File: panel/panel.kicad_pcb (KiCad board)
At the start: 4 copper layers, 36 x 36 mm, 289 parts, among them J1 IN, J2 OUT, Q1 Q_PMOS_GSD, Q10 Q_PMOS_GSD, Q11 Q_PMOS_GSD, Q12 Q_PMOS_GSD, Q13 Q_PMOS_GSD, Q14 Q_PMOS_GSD, Q15 Q_PMOS_GSD, Q16 Q_PMOS_GSD, Q2 Q_PMOS_GSD, Q3 Q_PMOS_GSD, Q4 Q_PMOS_GSD, Q5 Q_PMOS_GSD, Q6 Q_PMOS_GSD, Q7 Q_PMOS_GSD, Q8 Q_PMOS_GSD, Q9 Q_PMOS_GSD, U1 TLC59025, U2 TLC59025, U3 TLC59025, U4 SN74HC595, U5 SN74HC595, U6 NC7WZ17, U7 NC7WZ17

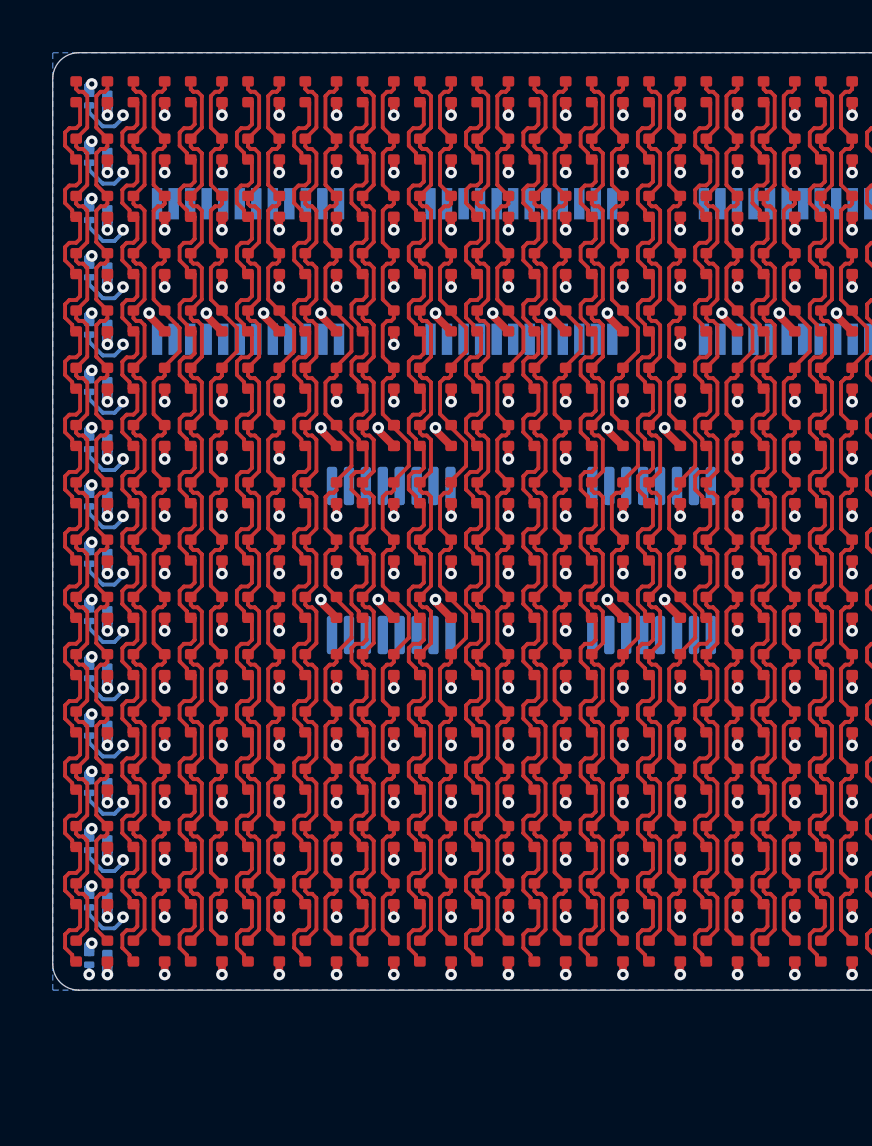
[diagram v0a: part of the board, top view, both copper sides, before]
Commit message: First option for row MOSFET layout
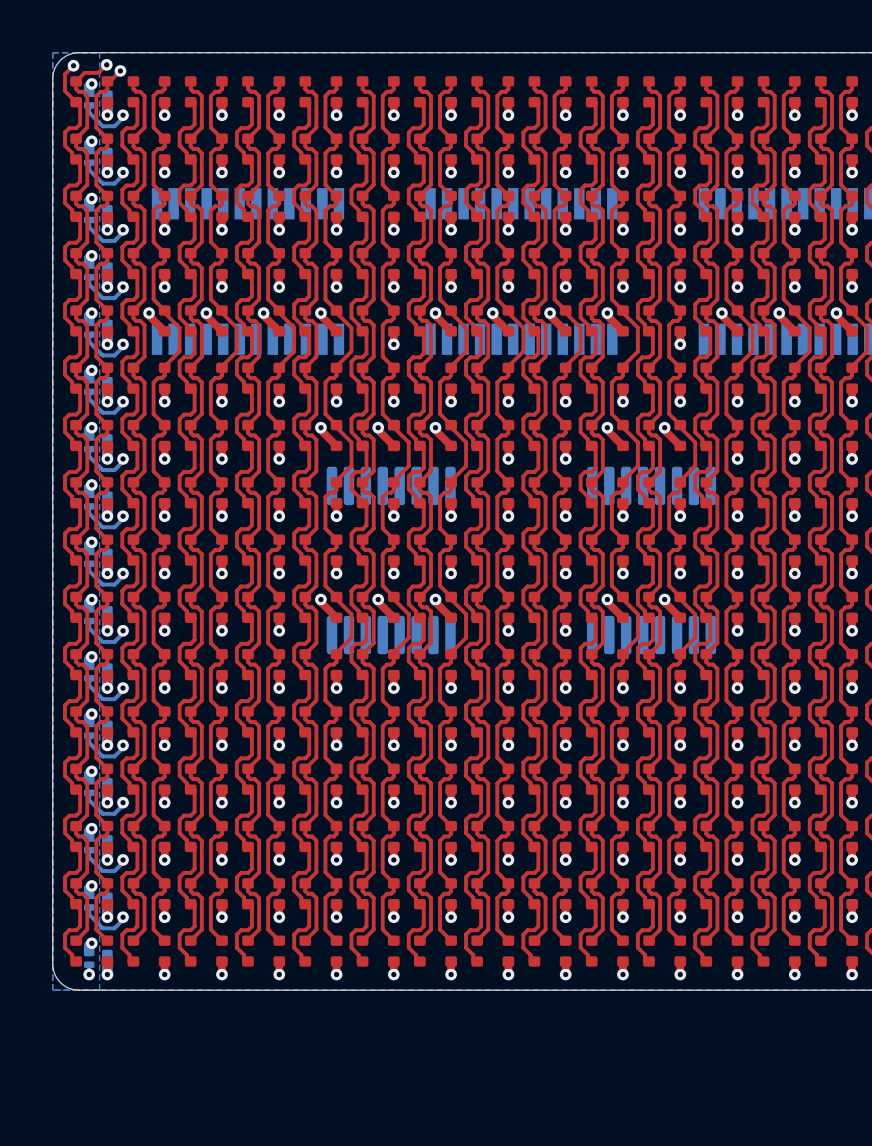
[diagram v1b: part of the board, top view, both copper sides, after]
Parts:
- turned U5 to 90 degrees
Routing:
- net COL_0B: track 45.1 -> 46.8 mm, vias 0 -> 1
- net COL_0G: track 39.7 -> 41.2 mm, vias 0 -> 1
- net COL_0R: track 39.7 -> 40.4 mm, vias 0 -> 1
- added copper zone on B.Cu, net VCC
- removed copper zone on In2.Cu, net VCC

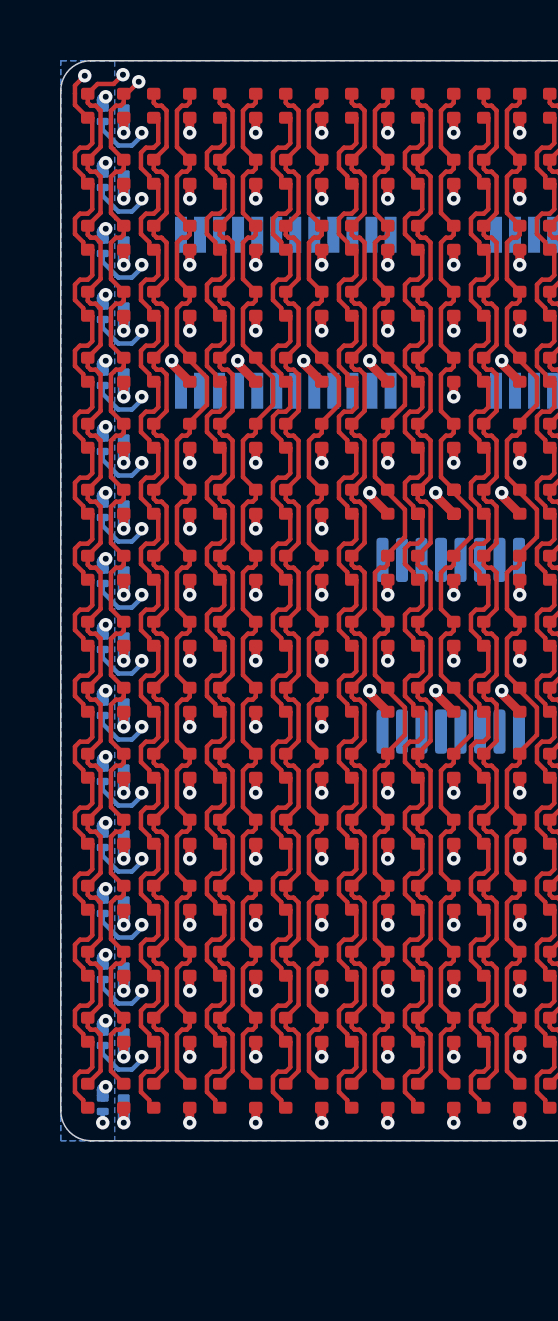
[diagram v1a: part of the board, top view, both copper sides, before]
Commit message: New strategy for powering rows
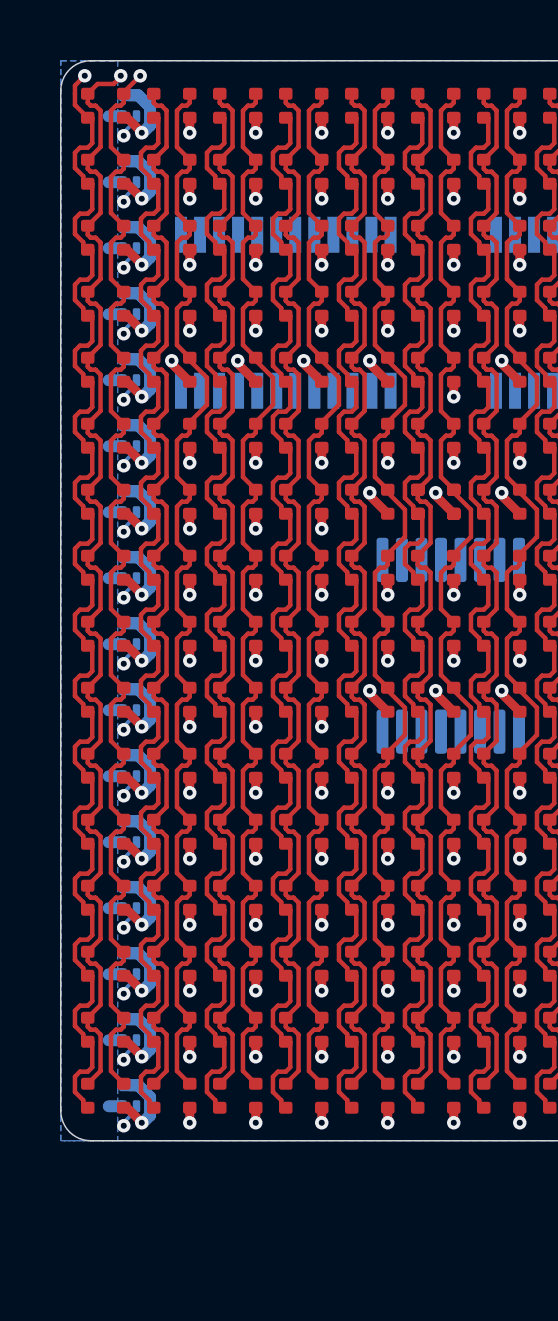
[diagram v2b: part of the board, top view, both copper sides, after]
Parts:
- moved Q14 0.63 mm to (62.3, 90.1), turned to 90 degrees
- moved Q4 0.63 mm to (62.3, 68.1), turned to 90 degrees
- moved Q9 0.63 mm to (62.3, 79.1), turned to 90 degrees
- moved Q1 0.63 mm to (62.3, 61.5), turned to 90 degrees
- moved Q10 0.63 mm to (62.3, 81.3), turned to 90 degrees
- moved Q11 0.63 mm to (62.3, 83.5), turned to 90 degrees
- moved Q12 0.63 mm to (62.3, 85.7), turned to 90 degrees
- moved Q13 0.63 mm to (62.3, 87.9), turned to 90 degrees
- moved Q15 0.63 mm to (62.3, 92.3), turned to 90 degrees
- moved Q16 0.63 mm to (62.3, 94.5), turned to 90 degrees
- moved Q2 0.63 mm to (62.3, 63.7), turned to 90 degrees
- moved Q3 0.63 mm to (62.3, 65.9), turned to 90 degrees
- moved Q5 0.63 mm to (62.3, 70.3), turned to 90 degrees
- moved Q6 0.63 mm to (62.3, 72.5), turned to 90 degrees
- moved Q7 0.63 mm to (62.3, 74.7), turned to 90 degrees
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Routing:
- net /ROW_8: track 2.03 -> 0.83 mm
- net /ROW_3: track 2.03 -> 0.83 mm
- net /ROW_13: track 2.03 -> 0.83 mm
- net /ROW_0: track 2.03 -> 0.83 mm
- net /ROW_7: track 2.03 -> 0.83 mm
- net /ROW_6: track 2.03 -> 0.83 mm
- net /ROW_2: track 2.03 -> 0.83 mm
- net /ROW_12: track 2.03 -> 0.83 mm
- net /ROW_11: track 2.03 -> 0.83 mm
- net /ROW_1: track 2.03 -> 0.83 mm
- net /ROW_9: track 2.03 -> 0.83 mm
- net /ROW_4: track 2.03 -> 0.83 mm
- net /ROW_14: track 2.03 -> 0.83 mm
- net /ROW_5: track 2.03 -> 0.83 mm
- net /ROW_10: track 2.03 -> 0.83 mm
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
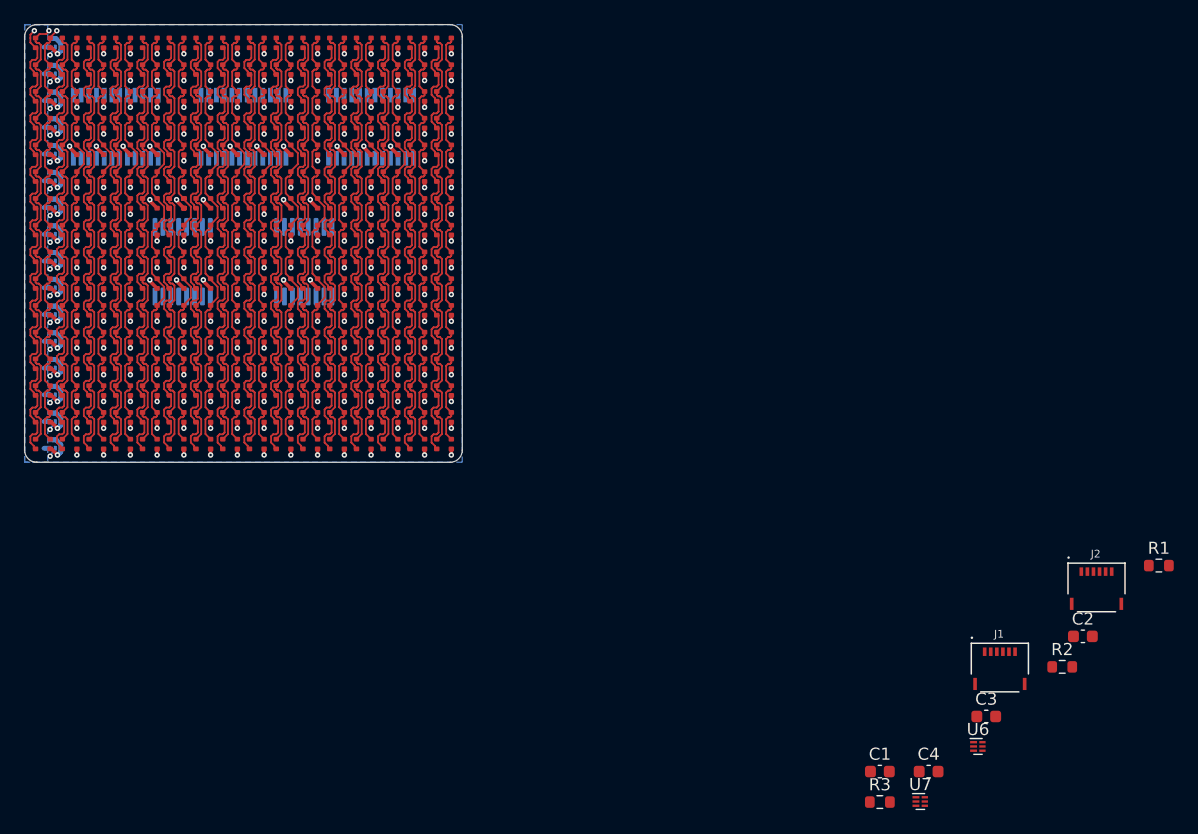
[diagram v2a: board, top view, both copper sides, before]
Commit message: Row gates 0-7 routed
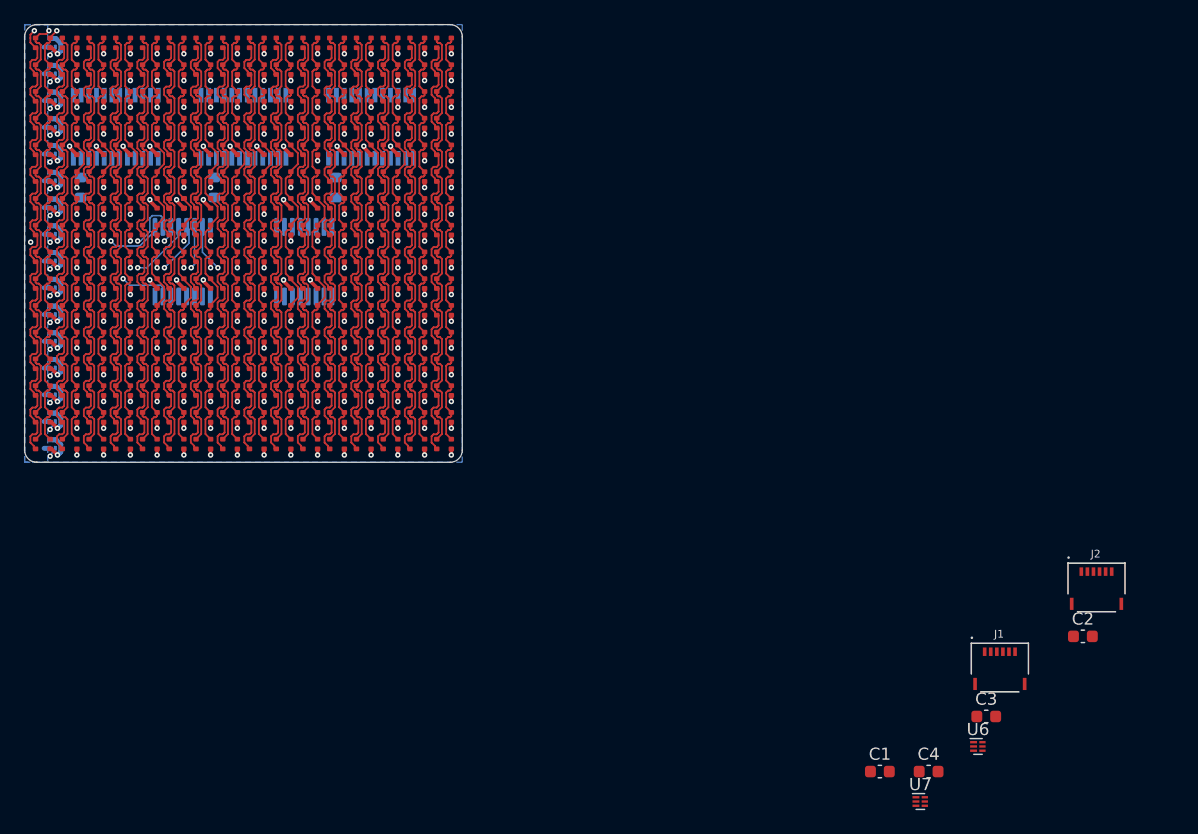
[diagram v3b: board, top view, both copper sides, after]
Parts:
- R1, R2, R3: moved to B.Cu
- moved R3 82.9 mm to (64.6, 73.4), turned to -90 degrees
- moved R2 80.1 mm to (75.6, 73.4), turned to -90 degrees
- moved R1 74.5 mm to (85.6, 73.4), turned to -90 degrees
- turned U4 to -90 degrees
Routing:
- net /ROW_0: track 0.83 -> 30.8 mm, vias 1 -> 3
- net /ROW_1: track 0.83 -> 23.9 mm, vias 1 -> 2
- net /ROW_2: track 0.83 -> 23.2 mm, vias 1 -> 2
- net /ROW_4: track 0.83 -> 22.2 mm, vias 1 -> 2
- net /ROW_5: track 0.83 -> 20.9 mm, vias 1 -> 2
- net /ROW_3: track 0.83 -> 19.8 mm, vias 1 -> 2
- net /ROW_6: track 0.83 -> 19.7 mm, vias 1 -> 2
- net /ROW_7: track 0.83 -> 19.5 mm, vias 1 -> 2

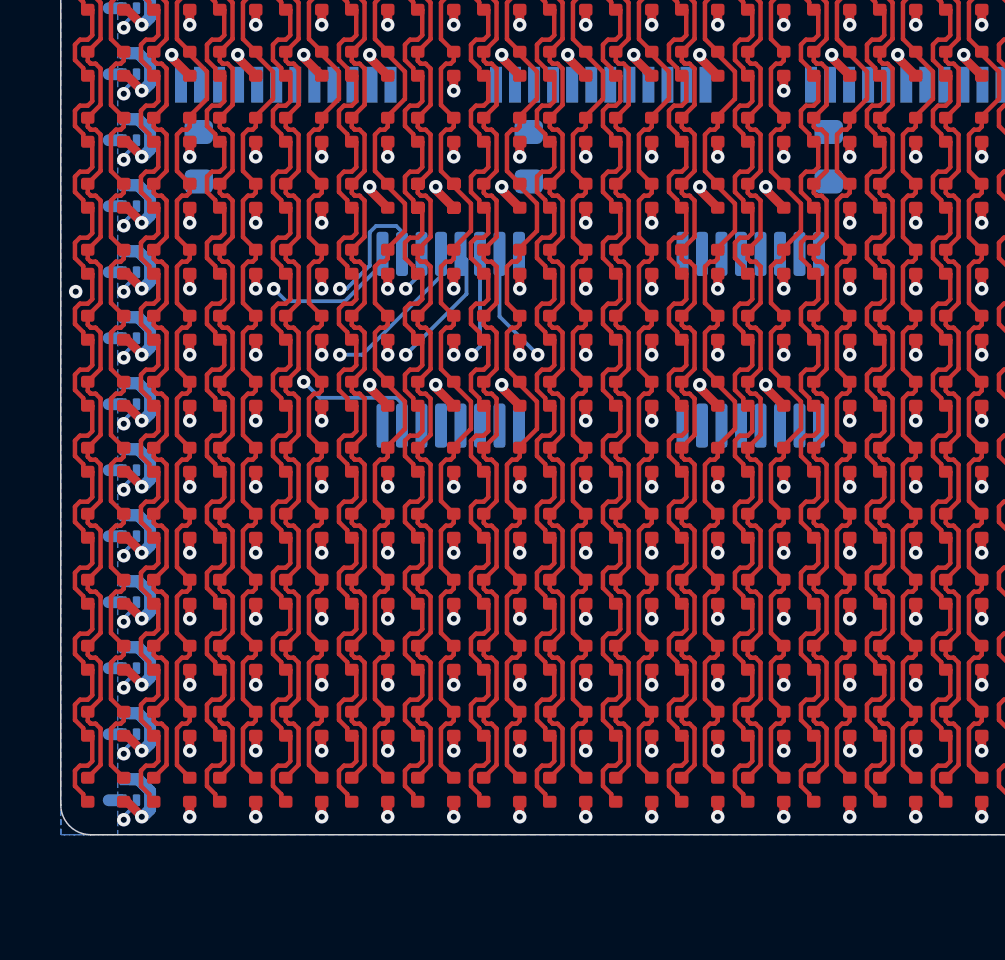
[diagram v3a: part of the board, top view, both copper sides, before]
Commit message: Rerouted first half of row drivers
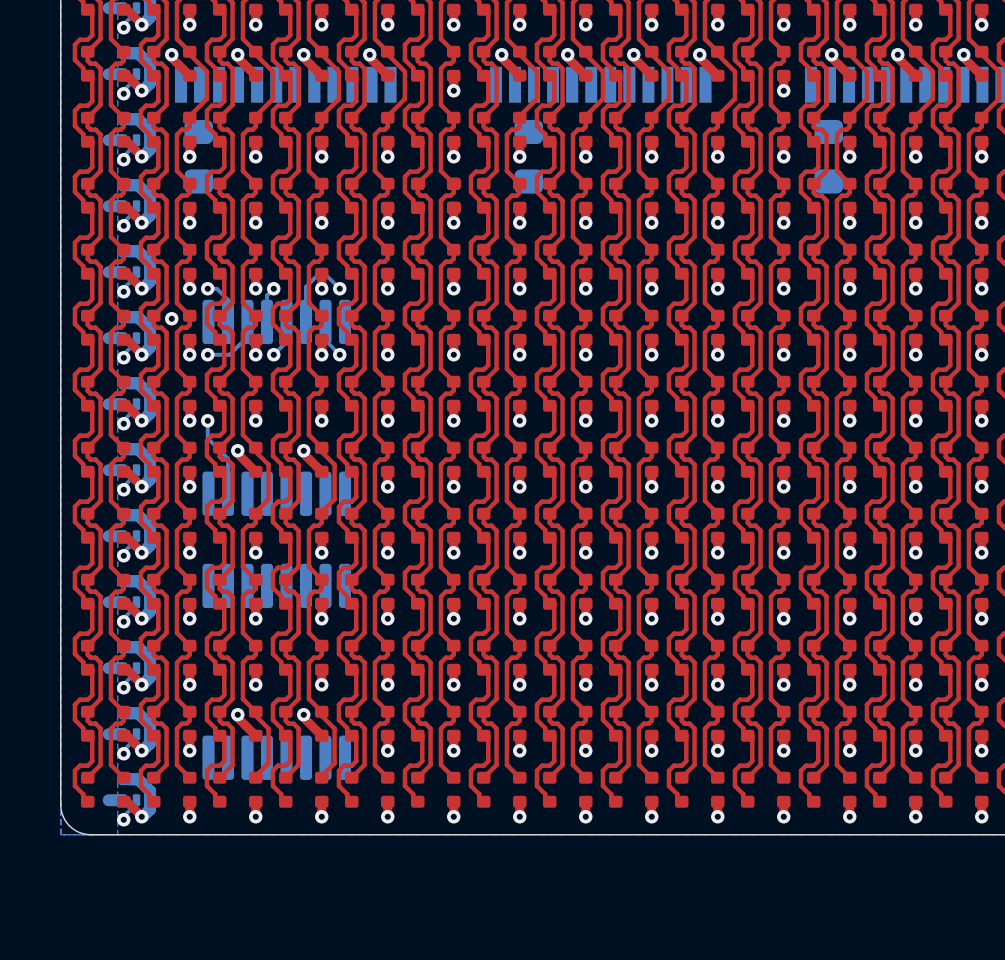
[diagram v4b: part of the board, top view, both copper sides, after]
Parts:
- moved U5 19.3 mm to (67.2, 90.6), turned to -90 degrees
- moved U4 6.23 mm to (67.2, 81.8)
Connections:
- U4 pad 10: VCC -> /ROW_9/COMMON
- U4 pad 11: /CLK -> /ROW_9/COMMON
- U4 pad 14: /DAT -> /ROW_9/COMMON
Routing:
- net /ROW_4: track 22.2 -> 13.1 mm
- net /ROW_6: track 19.7 -> 11.7 mm
- net /ROW_5: track 20.9 -> 13.1 mm
- net /ROW_7: track 19.5 -> 12.0 mm
- net /ROW_2: track 23.2 -> 16.0 mm
- net /ROW_1: track 23.9 -> 17.1 mm
- net /ROW_0: track 30.8 -> 25.6 mm, vias 3 -> 2
- net /ROW_3: track 19.8 -> 16.5 mm

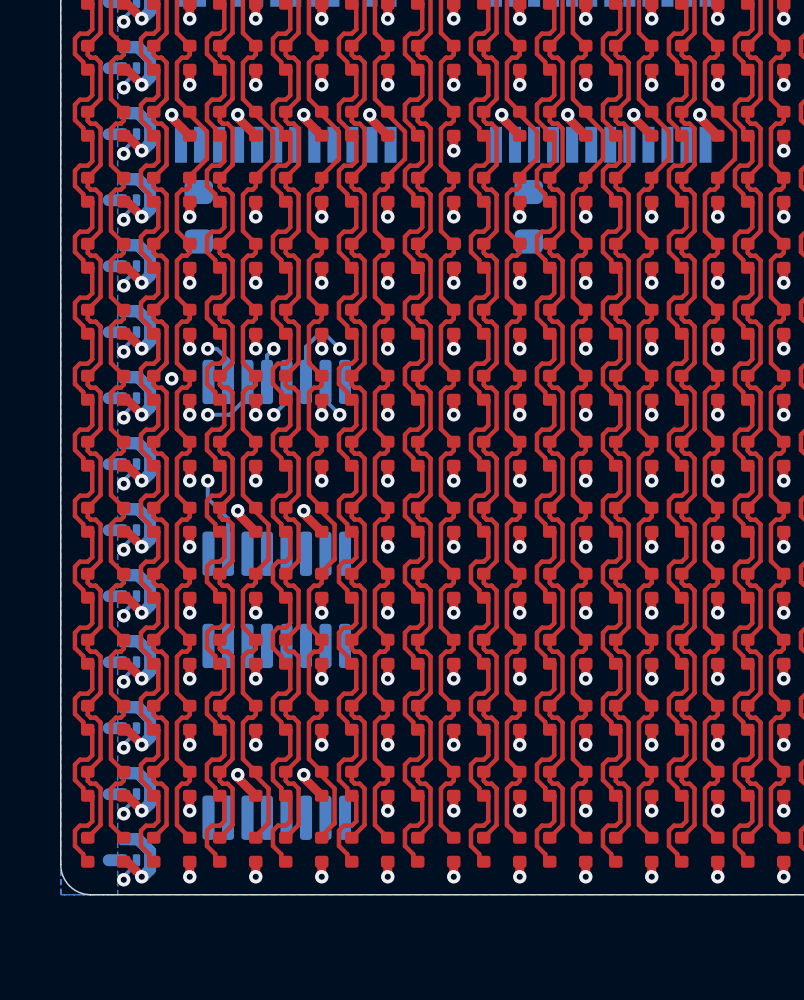
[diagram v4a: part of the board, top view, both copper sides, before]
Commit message: Routed second half of row drivers
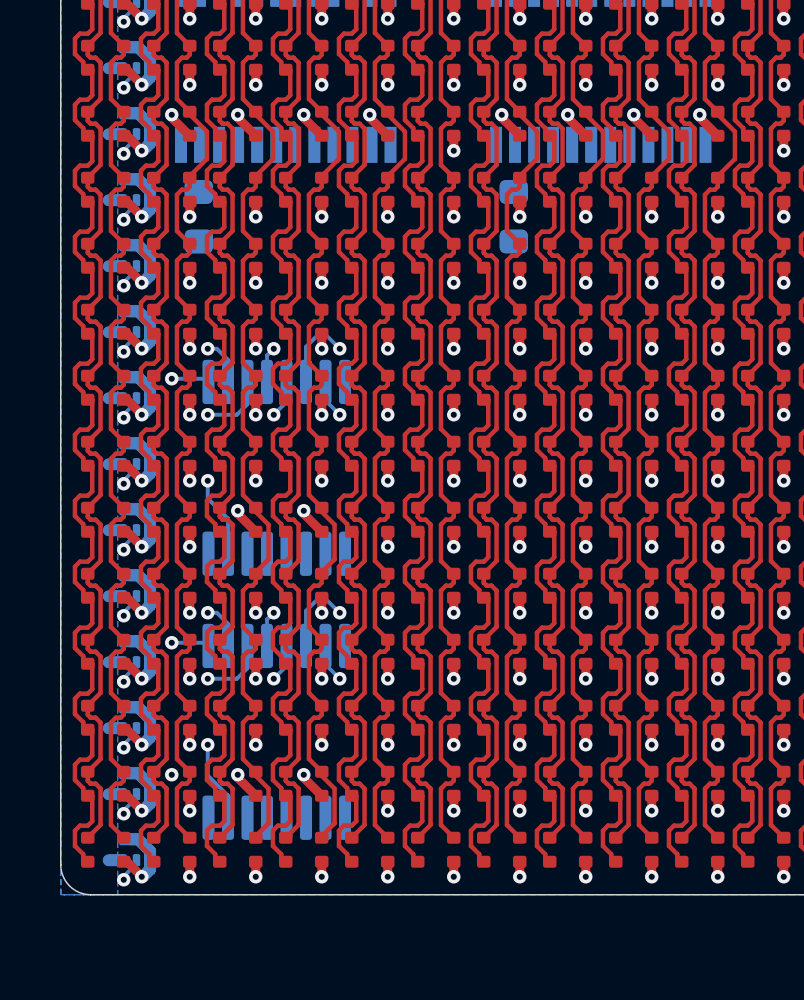
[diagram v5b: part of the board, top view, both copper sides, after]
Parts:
- removed the D102 at (72.5, 74.7)
- moved R2 0.50 mm to (75.1, 73.4)
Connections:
- U4 pad 10: /ROW_9/COMMON -> VCC
- U4 pad 11: /ROW_9/COMMON -> /CLK
- U4 pad 14: /ROW_9/COMMON -> /DAT
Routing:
- net /ROW_8: track 0.83 -> 24.8 mm, vias 1 -> 2
- net /ROW_15: track 0.83 -> 17.6 mm, vias 1 -> 2
- net /ROW_14: track 0.83 -> 14.1 mm, vias 1 -> 3
- net /ROW_13: track 0.83 -> 10.4 mm, vias 1 -> 2
- net /ROW_9: track 0.83 -> 9.16 mm, vias 1 -> 2
- net /ROW_12: track 0.83 -> 8.58 mm, vias 1 -> 2
- net /ROW_10: track 0.83 -> 6.90 mm, vias 1 -> 2
- net /ROW_11: track 0.83 -> 6.71 mm, vias 1 -> 2
- net /ROW_7: track 12.0 -> 10.2 mm
- net /ROW_1: track 17.1 -> 18.4 mm
